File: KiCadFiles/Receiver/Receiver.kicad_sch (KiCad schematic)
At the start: 2 parts, among them U2 NRF24L01_Breakout

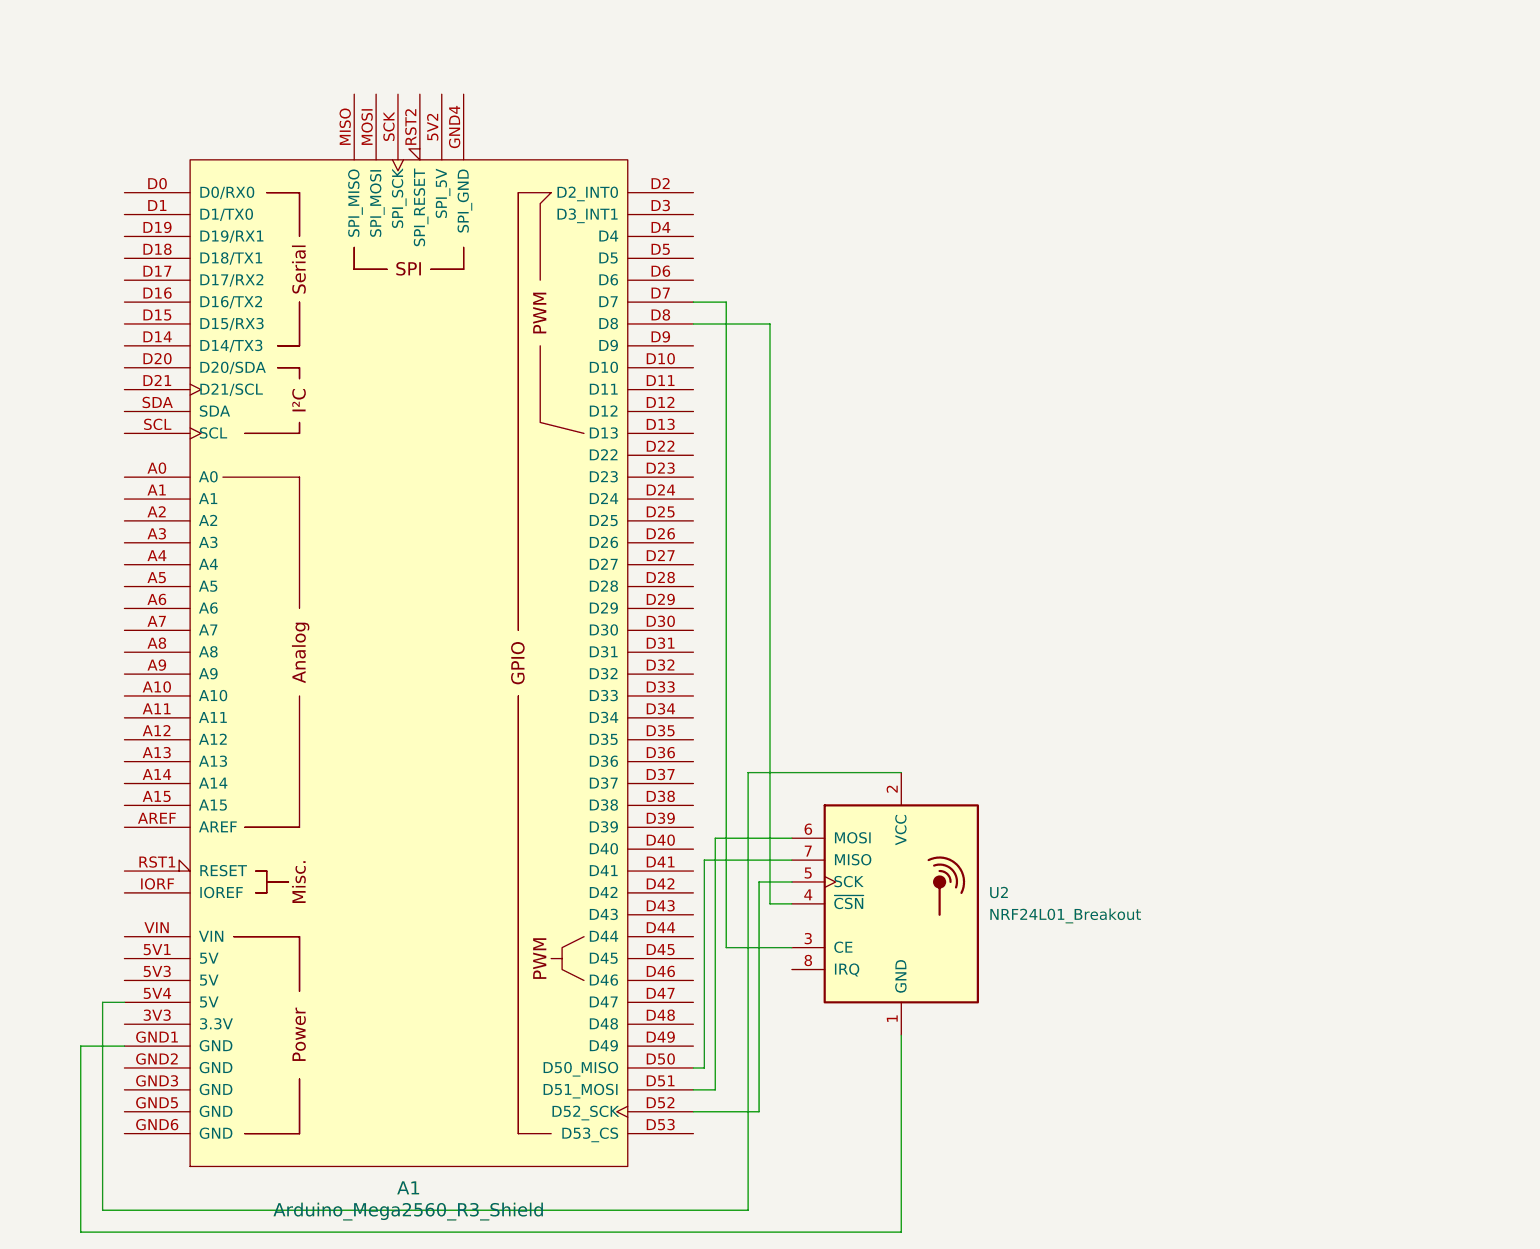
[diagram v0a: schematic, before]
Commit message: Update schematics and make car run
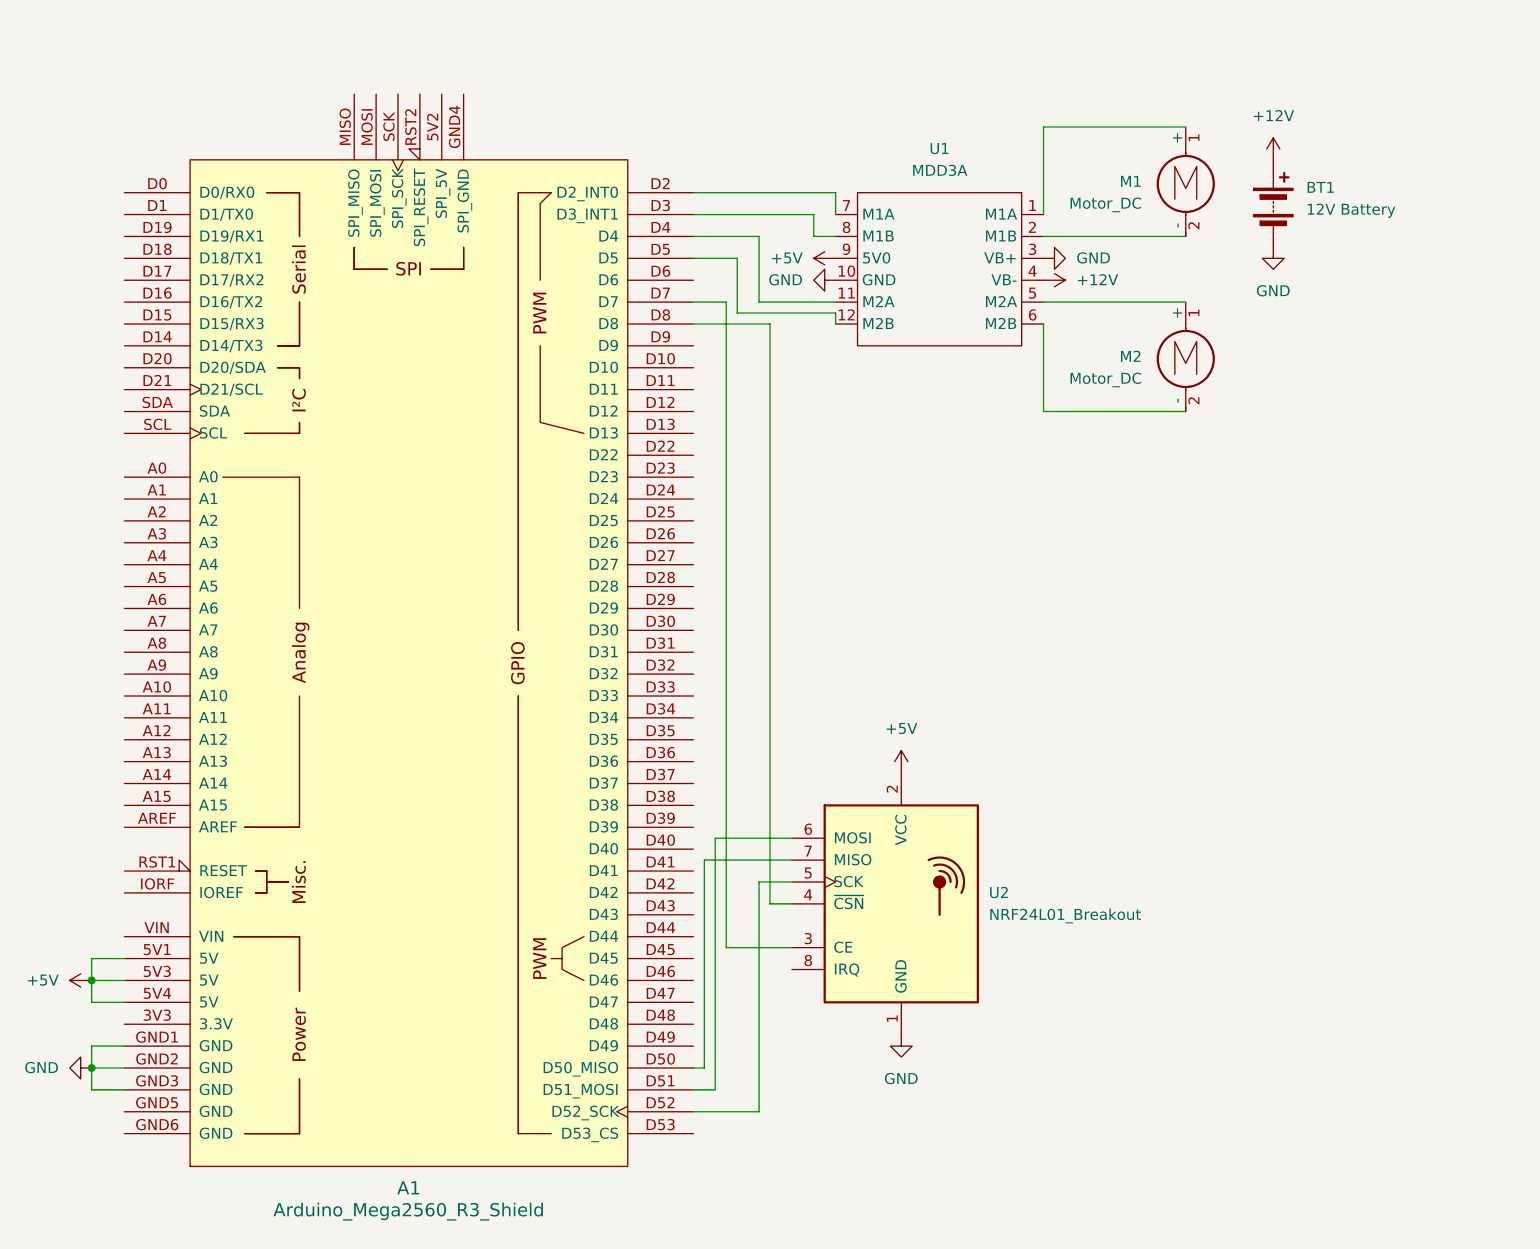
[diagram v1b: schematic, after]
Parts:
- added BT1: 12V Battery, symbol Device:Battery
- added M1, M2: Motor_DC, symbol Motor:Motor_DC
- added U1: MDD3A, symbol Breakout_Board_Library:MDD3A
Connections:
- net GND: now reaches A1.GND1 (GND), U2.1 (GND)
- net GND: now also A1.GND2 (GND), A1.GND3 (GND), BT1.2 (-), U1.10 (GND), U1.3 (VB+)
- net +5V: now reaches A1.5V4 (5V), U2.2 (VCC)
- net +5V: now also A1.5V1 (5V), A1.5V3 (5V), U1.9 (5V0)
- net at A1.D2 (D2_INT0): now also U1.7 (M1A)
- net at A1.D3 (D3_INT1): now also U1.8 (M1B)
- net at A1.D4: now also U1.11 (M2A)
- net at A1.D5: now also U1.12 (M2B)
- new net: M2.1 (+), U1.5 (M2A)
- new net: M2.2 (-), U1.6 (M2B)
- new net: M1.1 (+), U1.1 (M1A)
- new net: M1.2 (-), U1.2 (M1B)
- new net +12V: BT1.1 (+), U1.4 (VB-)

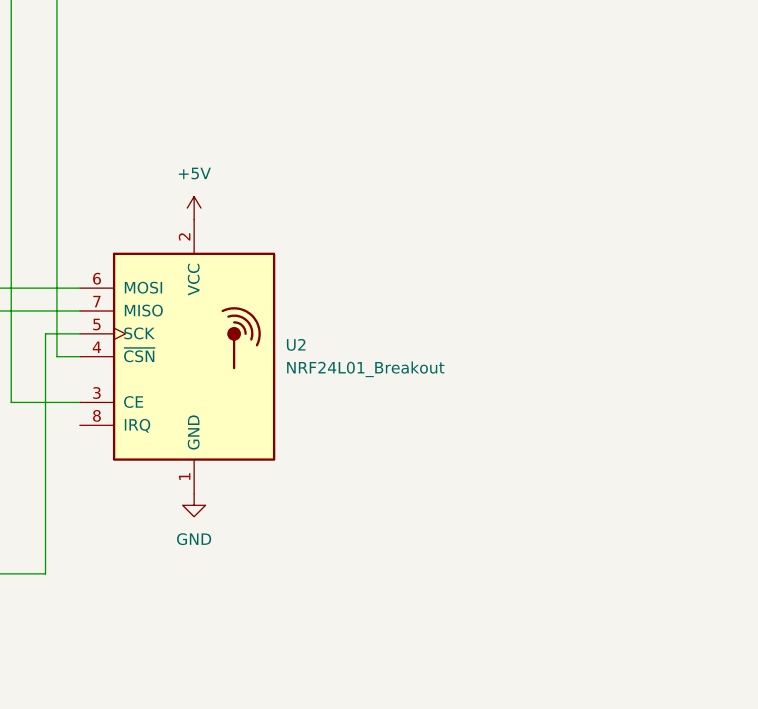
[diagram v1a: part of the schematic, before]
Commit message: Add more buttons, modify schematic, and change code (#6)
* Add more buttons, update schematic, improve drive system

* Change button pins, schematic, and add quarter speed
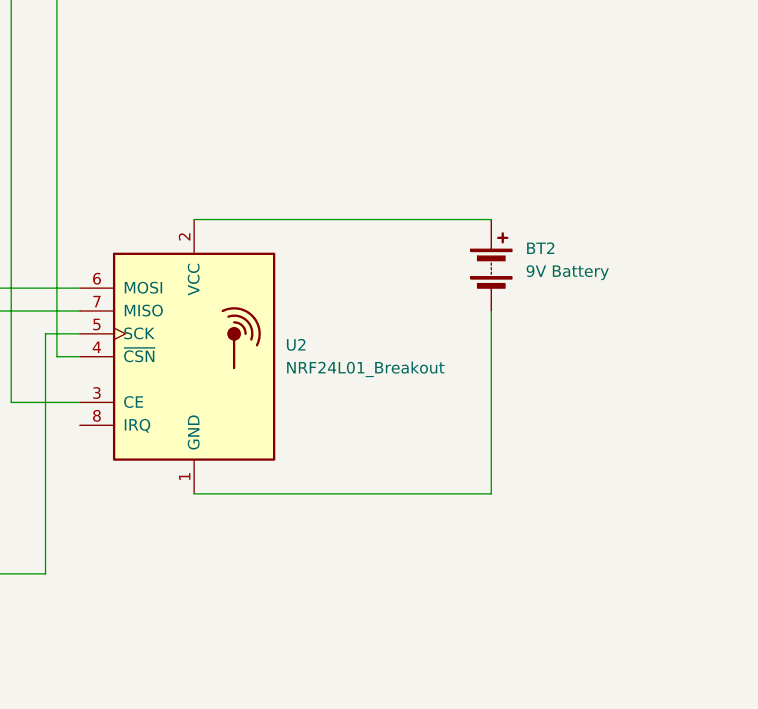
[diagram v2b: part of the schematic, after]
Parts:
- added BT2: 9V Battery, symbol Device:Battery
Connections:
- net +5V: no longer U2.2 (VCC)
- net GND: no longer U2.1 (GND)
- new net: BT2.1 (+), U2.2 (VCC)
- new net: BT2.2 (-), U2.1 (GND)

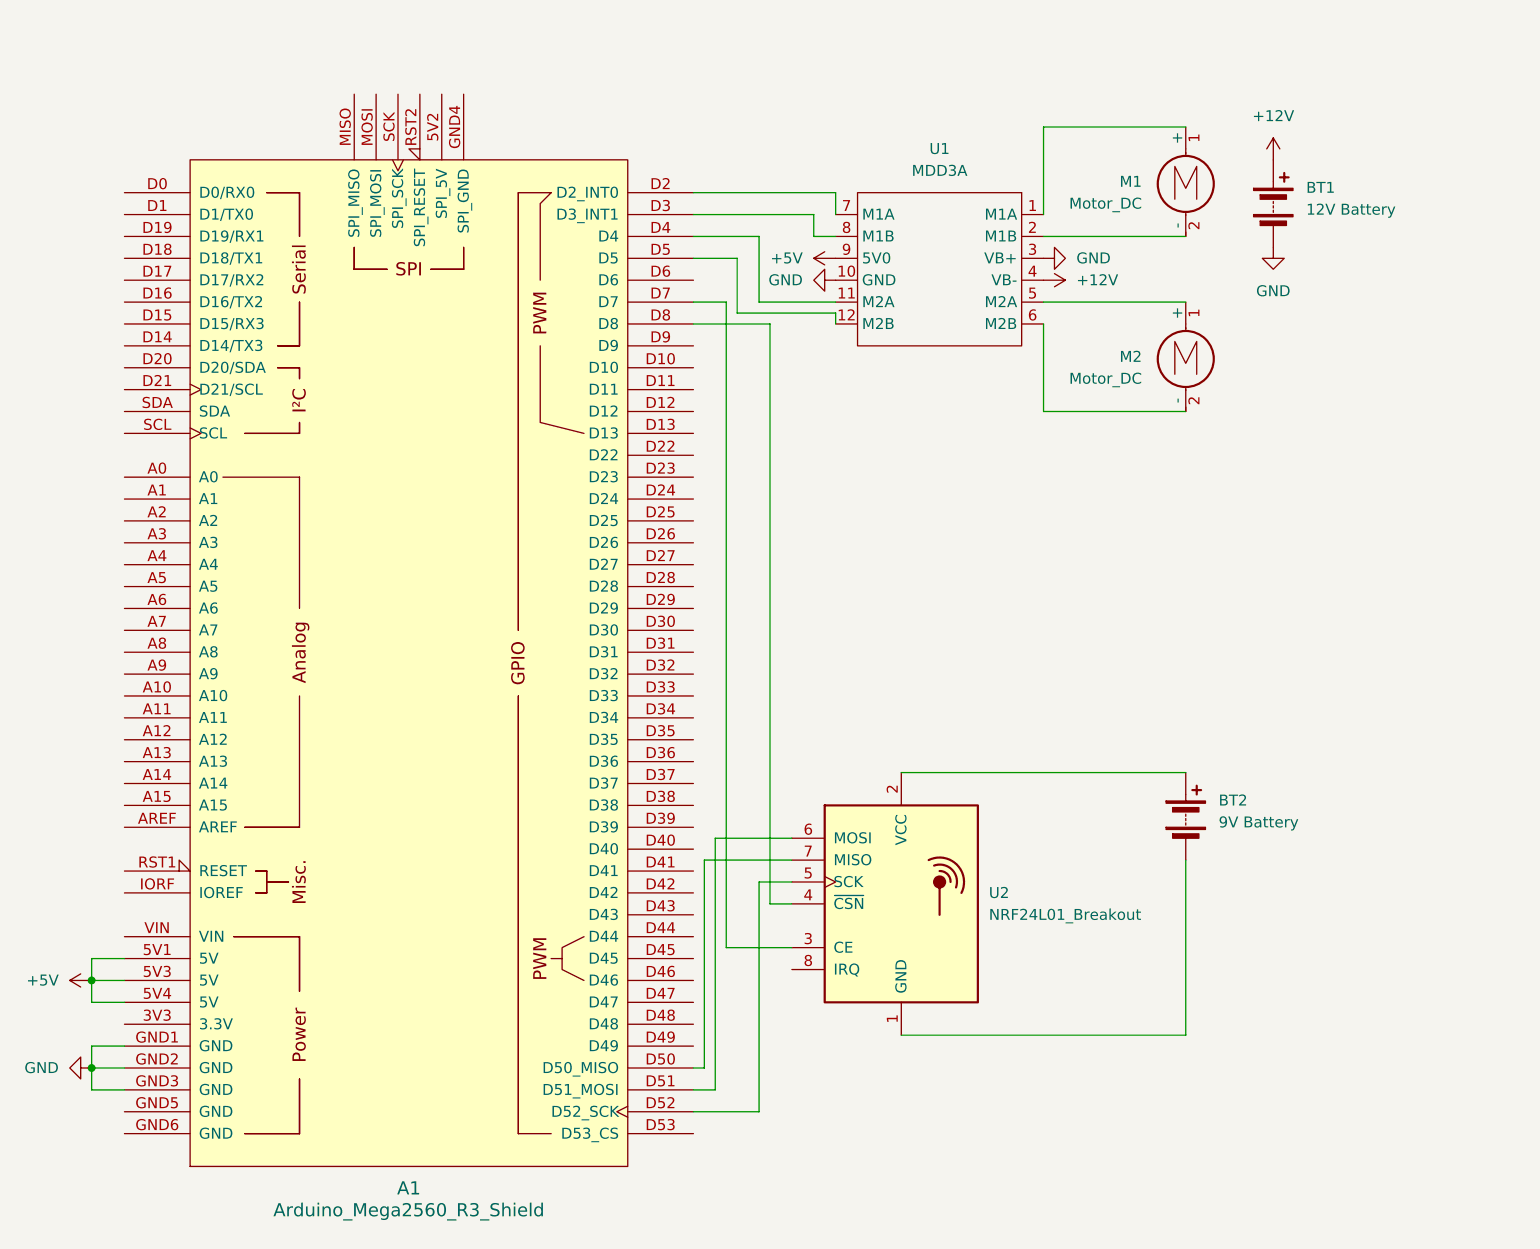
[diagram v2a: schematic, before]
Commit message: Add camera to robot (#7)
* Add camera code and schematic to upload code from Arduino UNO to camera

* Add camera to receiver schematic
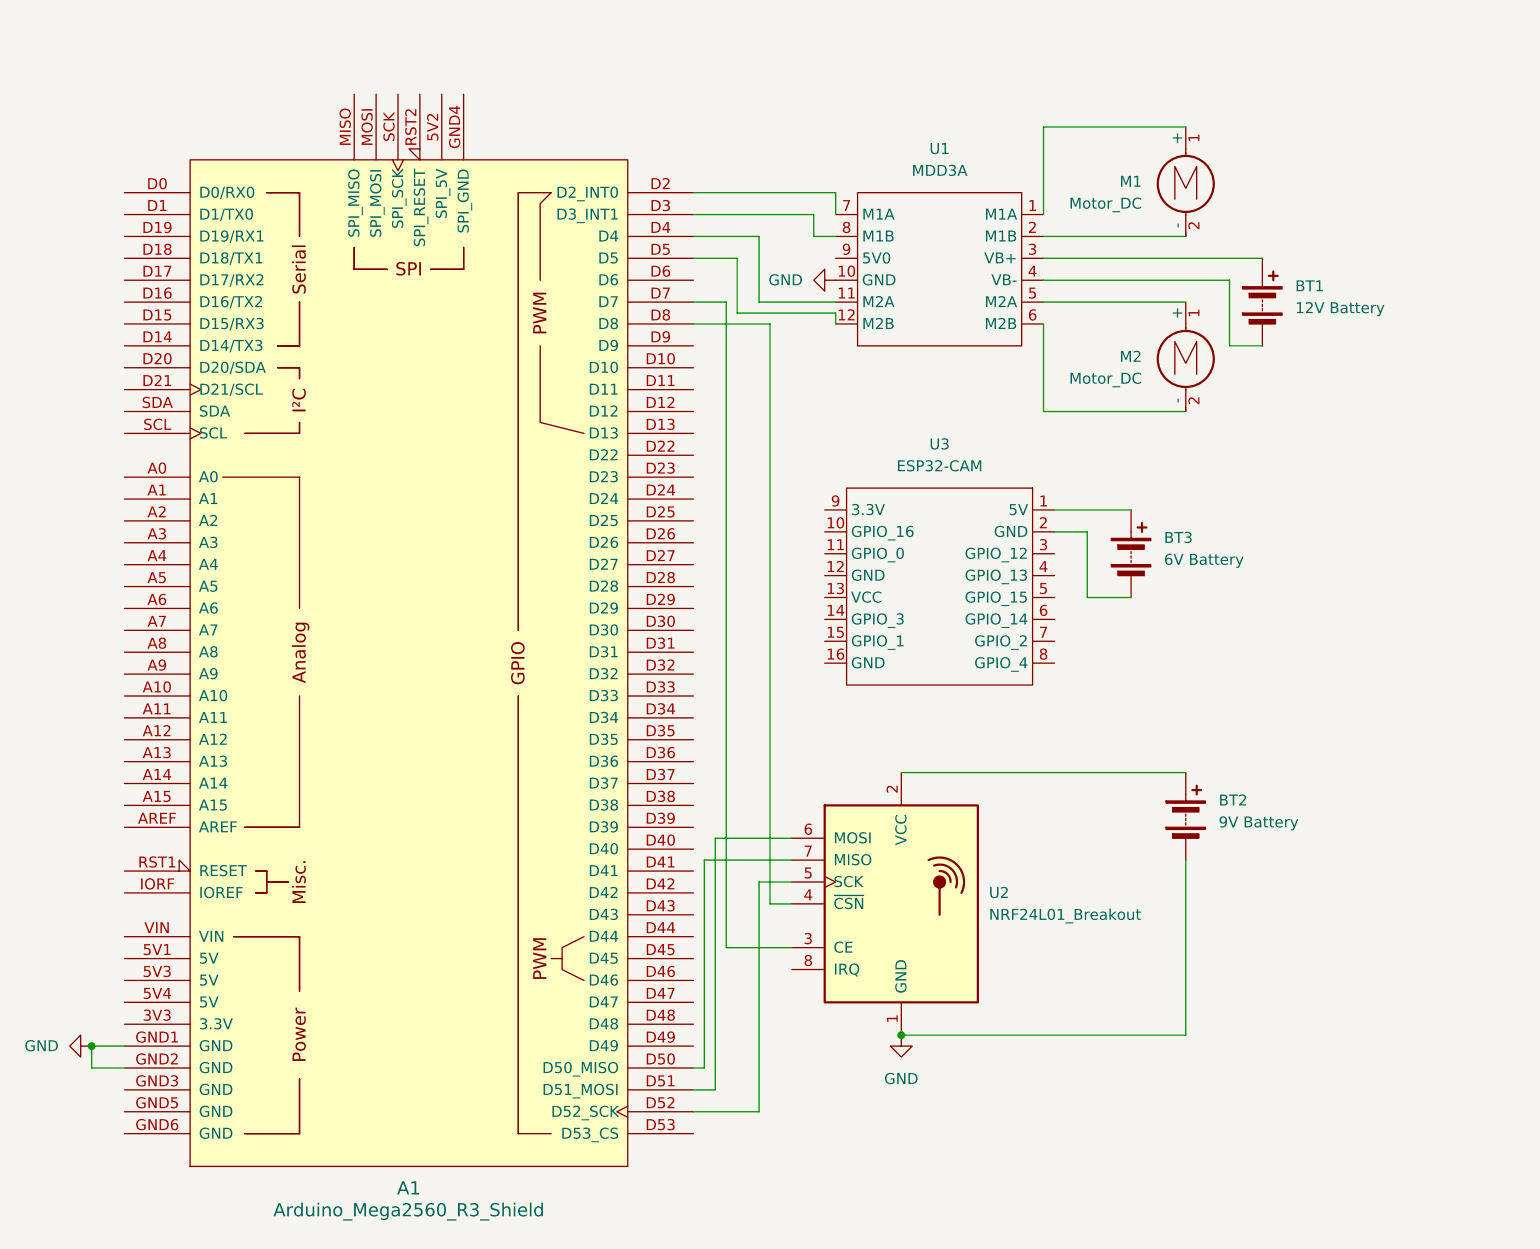
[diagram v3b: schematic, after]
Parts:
- added BT3: 6V Battery, symbol Device:Battery
- added U3: ESP32-CAM, symbol Microcontroller_Library:ESP32-CAM
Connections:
- net GND: now also BT2.2 (-), U2.1 (GND); no longer A1.GND3 (GND), BT1.2 (-), U1.3 (VB+)
- net +12V: no longer names the net of BT1.1 (+)
- net +12V: now also U1.3 (VB+); no longer U1.4 (VB-)
- removed net +5V: A1.5V1 (5V), A1.5V3 (5V), A1.5V4 (5V), U1.9 (5V0)
- new net: BT3.1 (+), U3.1 (5V)
- new net: BT3.2 (-), U3.2 (GND)
- new net: BT1.2 (-), U1.4 (VB-)
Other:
- moved on the sheet: BT1
